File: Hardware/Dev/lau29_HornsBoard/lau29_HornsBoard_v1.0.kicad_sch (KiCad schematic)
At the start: 18 parts, among them J1 Conn_01x03, J2 Conn_01x02, J3 Conn_01x02, J4 Conn_01x02, M1 MNMOS

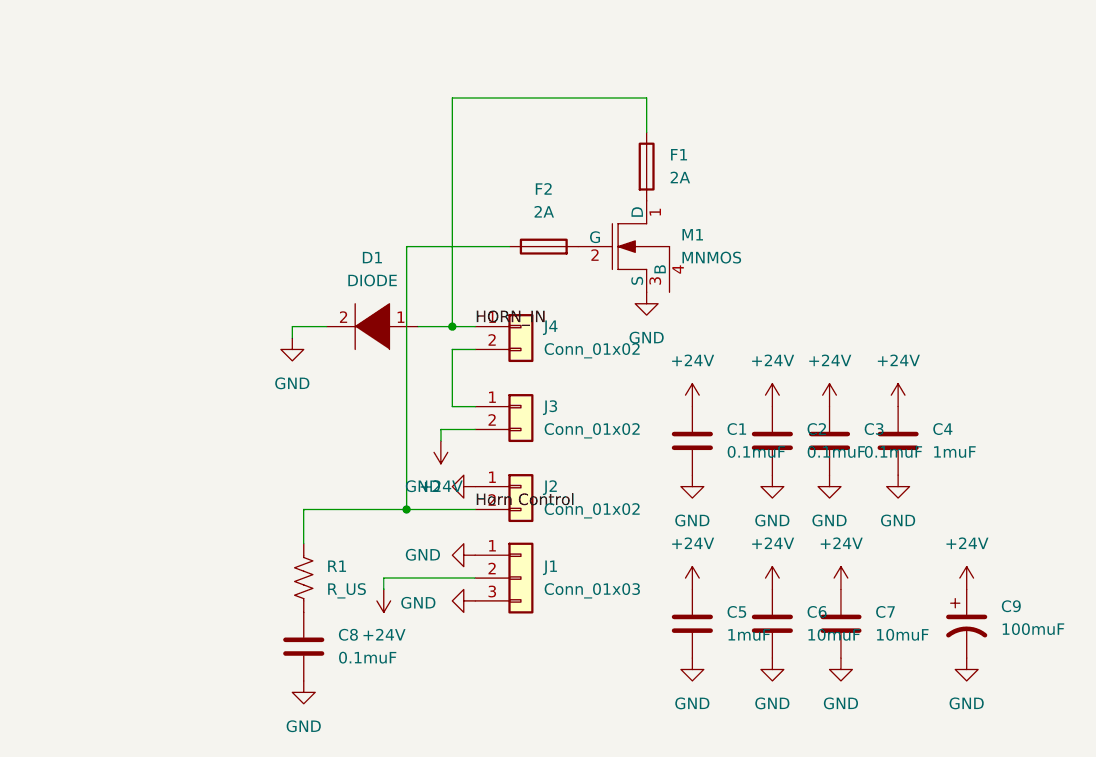
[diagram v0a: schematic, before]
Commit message: Fixed an error in firmware
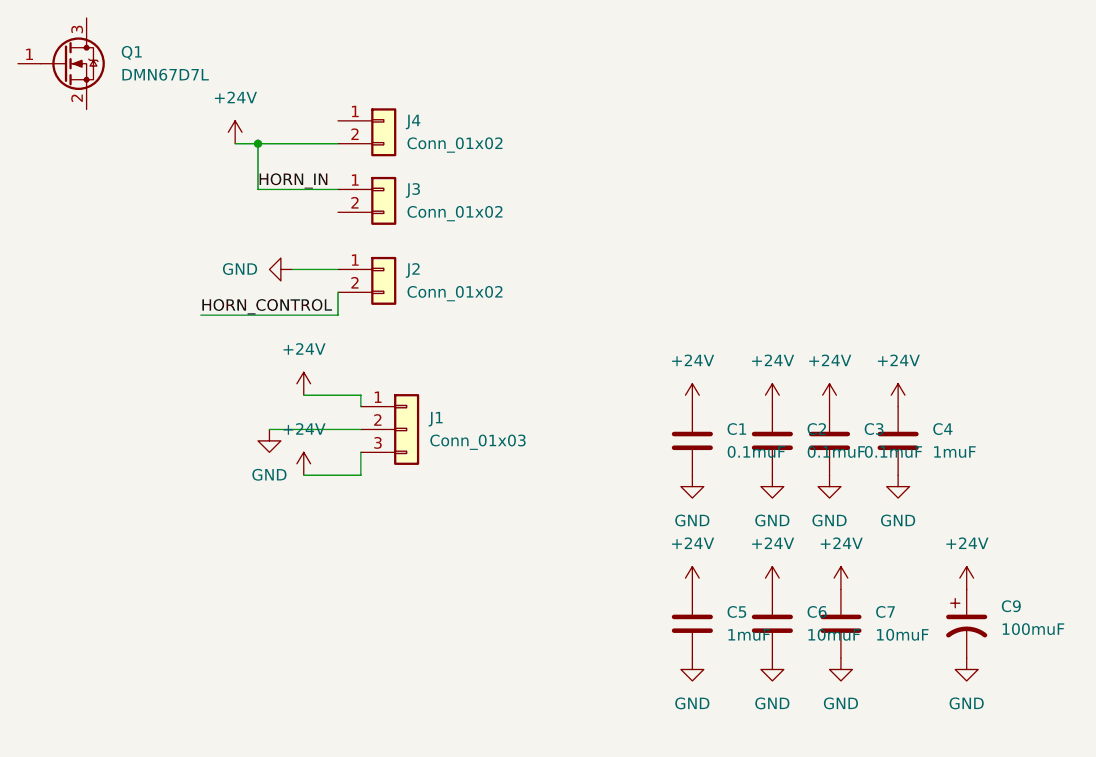
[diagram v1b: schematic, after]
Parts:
- removed C8: 0.1muF, symbol device:C
- removed D1: DIODE, symbol pspice:DIODE
- removed F1, F2: 2A, symbol device:Fuse
- removed M1: MNMOS, symbol pspice:MNMOS
- removed R1: R_US, symbol Device:R_US
- added Q1: DMN67D7L, Package_TO_SOT_SMD:SOT-23, symbol Transistor_FET:DMN67D7L
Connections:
- net +24V: now also J1.1 (Pin_1), J1.3 (Pin_3), J3.1 (Pin_1), J4.2 (Pin_2); no longer J1.2 (Pin_2), J3.2 (Pin_2)
- net GND: now also J1.2 (Pin_2); no longer J1.1 (Pin_1), J1.3 (Pin_3)
- net HORN_IN: no longer names the net of J4.1 (Pin_1)
- net Horn Control renamed HORN_CONTROL
